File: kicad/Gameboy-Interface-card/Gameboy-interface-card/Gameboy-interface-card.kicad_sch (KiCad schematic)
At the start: 35 parts, among them J1 SCREEN, J2 RASPBERRY_PI, J3 BATERY, Q1 NPN, SW1 BUTTON_A, SW2 BUTTON_B, SW3 BUTTON_SELECT, SW4 BUTTON_START, SW5 BUTTON_ARROW_UP, SW6 BUTTON_ARROW_DOWN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

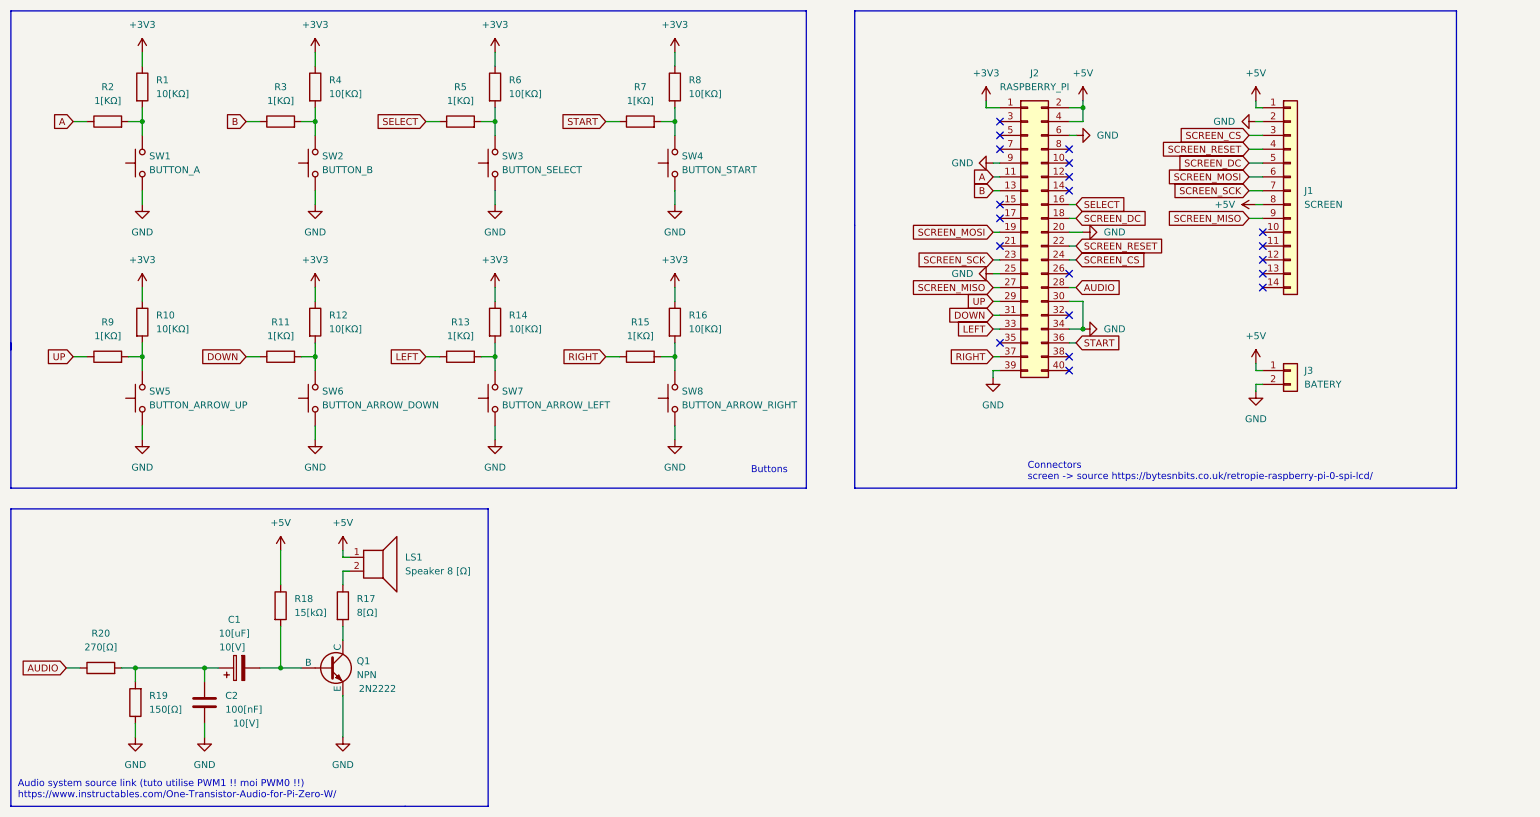
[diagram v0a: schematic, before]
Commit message: printed the pdf of the schematic and did the electrical rules check
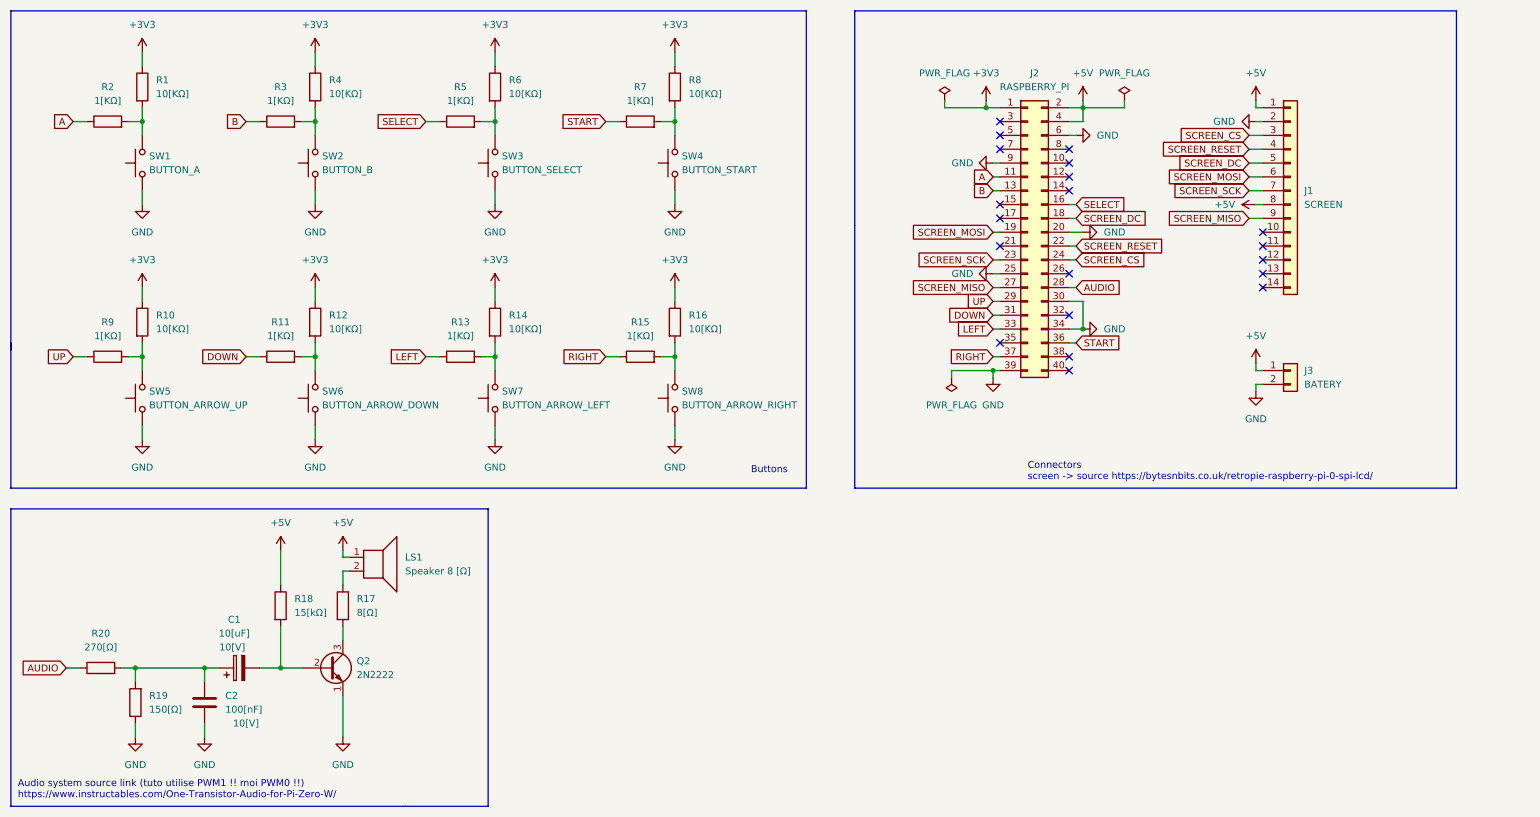
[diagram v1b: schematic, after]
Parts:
- removed Q1: NPN, symbol Simulation_SPICE:NPN
- added Q2: 2N2222, Package_TO_SOT_THT:TO-39-3, symbol Transistor_BJT:2N2219
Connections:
- net GND: now also Q2.1 (E)
- net at R17.2: now also Q2.3 (C)
- net at C1.2, R18.2: now also Q2.2 (B)
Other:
- company: (none) -> Maboey
- title: (none) -> Interface Card Gameboy-pi

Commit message: schema et emprintes terminees, pcb presque finit
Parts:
- C1: footprint (none) -> Capacitor_THT:CP_Radial_D4.0mm_P2.00mm; Value 2 10[V] -> (none)
- C2: footprint (none) -> Capacitor_SMD:C_0805_2012Metric; Value 2 10[V] -> (none)
- J1: footprint (none) -> Game_boy_PI:SCREEN_480X320_SPI
- J2: footprint (none) -> Game_boy_PI:RASPBERRY_PI_ZERO_W_2_BOTTOM
- J3: footprint (none) -> Game_boy_PI:DIY_BATTERY
- LS1: footprint (none) -> Game_boy_PI:HP_Gameboy
- Q2: footprint Package_TO_SOT_THT:TO-39-3 -> Package_TO_SOT_THT:TO-92_HandSolder
- R1, R10, R11, R12, R13, R14, R15, R16, R19, R2, R3, R4, R5, R6, R7, R8, R9: footprint (none) -> Resistor_SMD:R_0805_2012Metric_Pad1.20x1.40mm_HandSolder
- R17, R18, R20: footprint (none) -> Resistor_THT:R_Axial_DIN0207_L6.3mm_D2.5mm_P15.24mm_Horizontal
- SW1, SW2, SW3, SW4, SW5, SW6, SW7, SW8: footprint (none) -> Button_Switch_THT:SW_PUSH_6mm
